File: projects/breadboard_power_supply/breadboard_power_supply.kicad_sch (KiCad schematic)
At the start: 17 parts, among them J1 Barrel_Jack_Switch, J2 Conn_01x03_Pin, J3 Conn_01x02_Pin, J4 Screw_Terminal_01x02, J5 Conn_01x03_Pin, J6 Conn_01x02_Pin, J7 Screw_Terminal_01x02, U1 LM7805_TO220, U2 LM317_TO-220

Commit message: Organize libraries, add footprints (WIP)
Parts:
- removed S1: OS102011MS2QN1, OS102011MS2QN1:SW_OS102011MS2QN1, symbol OS102011MS2QN1:OS102011MS2QN1
- added S1: OS102011MS2QN1, Slide_Switch:SW_OS102011MS2QN1, symbol MH_Slide_Switch_OS102011MS2QN1:OS102011MS2QN1
- C1, C2, C3: footprint (none) -> Capacitor_SMD:C_0603_1608Metric_Pad1.08x0.95mm_HandSolder
- J1: footprint (none) -> Connector_BarrelJack:BarrelJack_Kycon_KLDX-0202-xC_Horizontal
- R1, R2, R3: footprint (none) -> Resistor_SMD:R_0603_1608Metric_Pad0.98x0.95mm_HandSolder
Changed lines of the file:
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@@
-	)
-	(symbol
-		(lib_id "OS102011MS2QN1:OS102011MS2QN1")
-		(at 80.01 57.15 90)
-		(unit 1)
-		(exclude_from_sim no)
-		(in_bom yes)
-		(on_board yes)
-		(dnp no)
-		(fields_autoplaced yes)
-		(property "Reference" "S1"
-			(at 85.09 56.0069 90)
-			(effects
-				(font
-					(size 1.27 1.27)
-				)
-				(justify right)
-			)
-		)
-		(property "Value" "OS102011MS2QN1"
-			(at 85.09 58.5469 90)
-			(effects
-				(font
-					(size 1.27 1.27)
-				)
-				(justify right)
-			)
-		)
-		(property "Footprint" "OS102011MS2QN1:SW_OS102011MS2QN1"
-			(at 80.01 57.15 0)
-			(effects
-				(font
-					(size 1.27 1.27)
-				)
-				(justify bottom)
-				(hide yes)
-			)
-		)
-		(property "Datasheet" ""
-			(at 80.01 57.15 0)
-			(effects
-				(font
-					(size 1.27 1.27)
-				)
-				(hide yes)
-			)
-		)
-		(property "Description" ""
-			(at 80.01 57.15 0)
-			(effects
-				(font
-					(size 1.27 1.27)
-				)
-				(hide yes)
-			)
-		)
-		(property "STANDARD" "MANUFACTURER RECOMMENDATIONS"
-			(at 80.01 57.15 0)
-			(effects
-				(font
-					(size 1.27 1.27)
-				)
-				(justify bottom)
-				(hide yes)
-			)
-		)
-		(property "MANUFACTURER" "C&K"
-			(at 80.01 57.15 0)
-			(effects
-				(font
-					(size 1.27 1.27)
-				)
-				(justify bottom)
-				(hide yes)
-			)
-		)
-		(pin "3"
-		)
-		(pin "2"
-		)
-		(pin "1"
-		)
-		(instances
-			(project ""
-				(path "/7d501a1c-ecfc-4b89-8a82-881c56ebfdf1"
-					(reference "S1")
-					(unit 1)
-				)
-			)
-		)
 	)
 	(symbol
@@
 			)
 		)
-		(property "Footprint" ""
+		(property "Footprint" "Capacitor_SMD:C_0603_1608Metric_Pad1.08x0.95mm_HandSolder"
 			(at 111.76 75.2348 0)
 			(effects
@@
 			)
 		)
-		(property "Footprint" ""
+		(property "Footprint" "Connector_BarrelJack:BarrelJack_Kycon_KLDX-0202-xC_Horizontal"
 			(at 53.34 64.516 0)
 			(effects
@@
 			)
 		)
-		(property "Footprint" ""
+		(property "Footprint" "Resistor_SMD:R_0603_1608Metric_Pad0.98x0.95mm_HandSolder"
 			(at 107.188 133.35 90)
 			(effects
@@
 			)
 		)
-		(property "Footprint" ""
+		(property "Footprint" "Resistor_SMD:R_0603_1608Metric_Pad0.98x0.95mm_HandSolder"
 			(at 58.928 129.54 90)
 			(effects
@@
 			)
 		)
-		(property "Footprint" ""
+		(property "Footprint" "Capacitor_SMD:C_0603_1608Metric_Pad1.08x0.95mm_HandSolder"
 			(at 137.16 75.2348 0)
 			(effects
@@
 			)
 		)
-		(property "Footprint" ""
+		(property "Footprint" "Resistor_SMD:R_0603_1608Metric_Pad0.98x0.95mm_HandSolder"
 			(at 107.188 149.86 90)
 			(effects
@@
 			)
 		)
-		(property "Footprint" ""
+		(property "Footprint" "Capacitor_SMD:C_0603_1608Metric_Pad1.08x0.95mm_HandSolder"
 			(at 113.03 117.1448 0)
 			(effects
@@
 					(unit 1)
 				)
+			)
+		)
+	)
+	(symbol
+		(lib_id "MH_Slide_Switch_OS102011MS2QN1:OS102011MS2QN1")
+		(at 77.47 59.69 0)
+		(unit 1)
+		(exclude_from_sim no)
+		(in_bom yes)
+		(on_board yes)
+		(dnp no)
+		(fields_autoplaced yes)
+		(property "Reference" "S1"
+			(at 81.28 58.4199 0)
+			(effects
+				(font
+					(size 1.27 1.27)
+				)
+				(justify left)
+			)
+		)
+		(property "Value" "OS102011MS2QN1"
+			(at 81.28 60.9599 0)
+			(effects
+				(font
+					(size 1.27 1.27)
+				)
+				(justify left)
+			)
+		)
+		(property "Footprint" "Slide_Switch:SW_OS102011MS2QN1"
+			(at 77.47 59.69 0)
+			(effects
+				(font
+					(size 1.27 1.27)
+				)
+				(justify bottom)
+				(hide yes)
+			)
+		)
+		(property "Datasheet" ""
+			(at 77.47 59.69 0)
+			(effects
+				(font
+					(size 1.27 1.27)
+				)
+				(hide yes)
+			)
+		)
+		(property "Description" ""
+			(at 77.47 59.69 0)
+			(effects
+				(font
+					(size 1.27 1.27)
+				)
+				(hide yes)
+			)
+		)
+		(property "STANDARD" "MANUFACTURER RECOMMENDATIONS"
+			(at 77.47 59.69 0)
+			(effects
+				(font
+					(size 1.27 1.27)
+				)
+				(justify bottom)
+				(hide yes)
+			)
+		)
+		(property "MANUFACTURER" "C&K"
+			(at 77.47 59.69 0)
+			(effects
+				(font
+					(size 1.27 1.27)
+				)
+				(justify bottom)
+				(hide yes)
+			)
+		)
+		(pin "3"
+		)
+		(pin "1"
+		)
+		(pin "2"
+		)
+		(instances
+			(project ""
+				(path "/7d501a1c-ecfc-4b89-8a82-881c56ebfdf1"
+					(reference "S1")
+					(unit 1)
+				)

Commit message: Best practices for libraries in breadboard_power_supply project
- move libraries/ folder inside main project folder
- make paths references relative using ${KIPRJMOD} variable
- modify .gitignore to commit fp-lib-table and sym-lib-table
- update links to MH_Slider_Switch symbol and footprint in KiCAD files
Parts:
- S1: footprint Slide_Switch:SW_OS102011MS2QN1 -> MH_Slide_Switch:SW_OS102011MS2QN1; symbol MH_Slide_Switch_OS102011MS2QN1:OS102011MS2QN1 -> MH_Slide_Switch:OS102011MS2QN1
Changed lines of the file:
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@@
 	)
 	(symbol
-		(lib_id "MH_Slide_Switch_OS102011MS2QN1:OS102011MS2QN1")
+		(lib_id "MH_Slide_Switch:OS102011MS2QN1")
 		(at 77.47 59.69 0)
 		(unit 1)
@@
 			)
 		)
-		(property "Footprint" "Slide_Switch:SW_OS102011MS2QN1"
+		(property "Footprint" "MH_Slide_Switch:SW_OS102011MS2QN1"
 			(at 77.47 59.69 0)
 			(effects

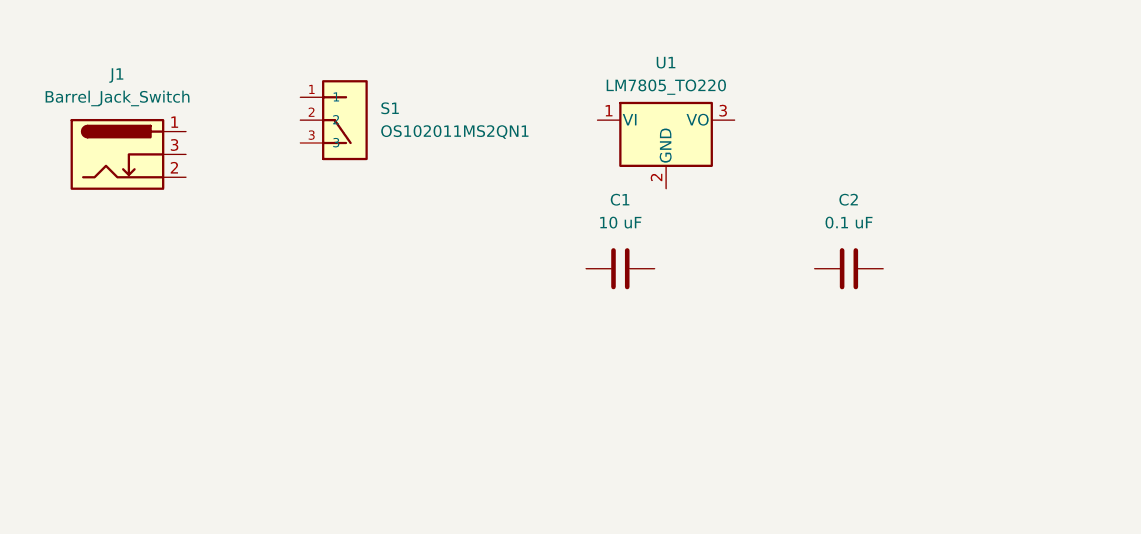
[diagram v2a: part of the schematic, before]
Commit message: Complete associations, start wiring
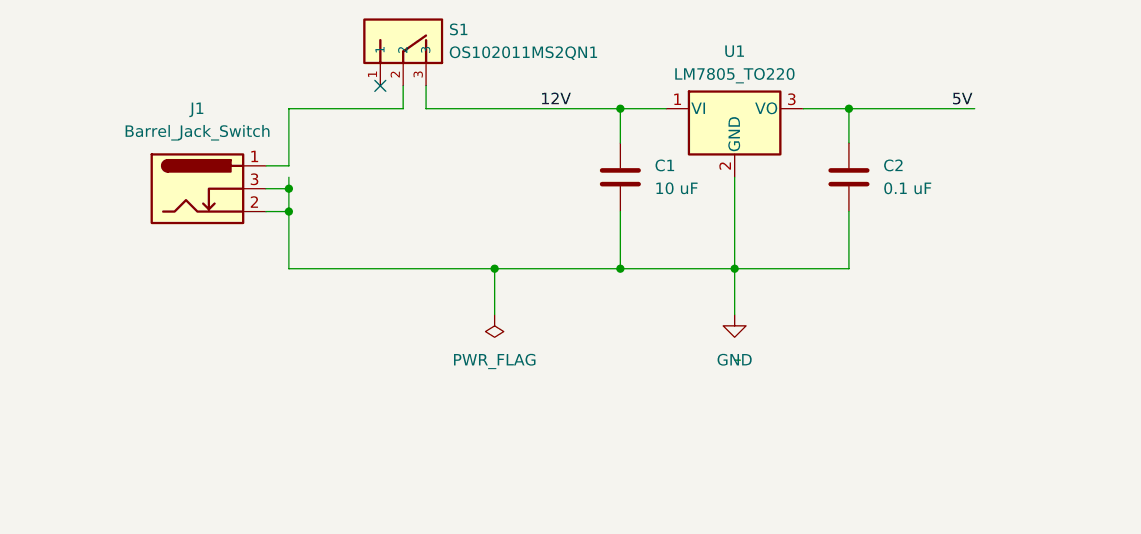
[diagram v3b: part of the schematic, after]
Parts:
- D1: footprint (none) -> LED_THT:LED_D5.0mm
- J2, J5: footprint (none) -> Connector_PinHeader_2.54mm:PinHeader_1x03_P2.54mm_Horizontal
- J3, J6: footprint (none) -> Connector_PinHeader_2.54mm:PinHeader_1x02_P2.54mm_Vertical
- J4, J7: footprint (none) -> TerminalBlock:TerminalBlock_bornier-2_P5.08mm
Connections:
- net GND: now reaches C1.1
- net GND: now also C2.1, J1.2, J1.3, U1.2 (GND)
- net 12V: now reaches C1.2
- net 12V: now also S1.3, U1.1 (VI)
- net at J1.1: now also S1.2
- net 5V: now reaches U1.3 (VO)
- net 5V: now also C2.2
- no-connect marks 0 -> 1
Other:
- moved on the sheet: C1, C2, J1, S1, U1

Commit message: Complete wiring
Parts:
- renumbered J7 to J6, J6 to J7, U2 to U1, U1 to U2
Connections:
- net 12V: now also R1.1, S1.1, U1.3 (VI); no longer S1.3
- net 5V: now also J2.3 (Pin_3), J5.3 (Pin_3)
- net GND: now also C3.1, D1.1 (K), J3.1 (Pin_1), J4.1 (Pin_1), J6.1 (Pin_1), J7.1 (Pin_1), R3.1
- net at J7.2 (Pin_2): now also J5.2 (Pin_2), J6.2 (Pin_2)
- net 3.3V: now reaches J5.1 (Pin_1)
- net 3.3V: now also C3.2, J2.1 (Pin_1), R2.2, U1.2 (VO)
- net at J2.2 (Pin_2): now also J3.2 (Pin_2), J4.2 (Pin_2)
- net at R2.1: now also R3.2, U1.1 (ADJ)
- net at R1.2: now also D1.2 (A)
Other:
- moved on the sheet: C1, C2, C3, D1, J1, J2, J3, J4, J5, J6, J7, R1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

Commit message: Name Nets
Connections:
- net PWR_output: now reaches J5.2 (Pin_2), J6.2 (Pin_2), J7.2 (Pin_2)
- net PWR_output: now also J2.2 (Pin_2), J3.2 (Pin_2), J4.2 (Pin_2)
- net PWR_input: now reaches J1.1, S1.2
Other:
- moved on the sheet: D1
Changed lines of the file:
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@@
 	)
 	(junction
-		(at 179.07 71.12)
+		(at 180.34 71.12)
 		(diameter 0)
 		(color 0 0 0 0)
@@
 	)
 	(junction
-		(at 184.15 59.69)
+		(at 185.42 59.69)
 		(diameter 0)
 		(color 0 0 0 0)
@@
 	(wire
 		(pts
-			(xy 179.07 62.23) (xy 190.5 62.23)
+			(xy 180.34 62.23) (xy 190.5 62.23)
 		)
 		(stroke
@@
 	(wire
 		(pts
-			(xy 179.07 71.12) (xy 190.5 71.12)
+			(xy 180.34 71.12) (xy 190.5 71.12)
 		)
 		(stroke
@@
 	(wire
 		(pts
-			(xy 184.15 46.99) (xy 184.15 59.69)
-		)
-		(stroke
-			(width 0)
-			(type default)
-		)
-	)
-	(wire
-		(pts
-			(xy 190.5 46.99) (xy 184.15 46.99)
+			(xy 185.42 46.99) (xy 185.42 59.69)
+		)
+		(stroke
+			(width 0)
+			(type default)
+		)
+	)
+	(wire
+		(pts
+			(xy 190.5 46.99) (xy 185.42 46.99)
 		)
 		(stroke
@@
 	(wire
 		(pts
-			(xy 179.07 62.23) (xy 179.07 71.12)
-		)
-		(stroke
-			(width 0)
-			(type default)
-		)
-	)
-	(wire
-		(pts
-			(xy 184.15 68.58) (xy 190.5 68.58)
+			(xy 180.34 62.23) (xy 180.34 71.12)
+		)
+		(stroke
+			(width 0)
+			(type default)
+		)
+	)
+	(wire
+		(pts
+			(xy 185.42 68.58) (xy 190.5 68.58)
 		)
 		(stroke
@@
 	(wire
 		(pts
-			(xy 179.07 71.12) (xy 179.07 77.47)
+			(xy 180.34 71.12) (xy 180.34 77.47)
 		)
 		(stroke
@@
 	(wire
 		(pts
-			(xy 184.15 59.69) (xy 190.5 59.69)
+			(xy 185.42 59.69) (xy 190.5 59.69)
 		)
 		(stroke
@@
 	(wire
 		(pts
-			(xy 184.15 59.69) (xy 184.15 68.58)
-		)
-		(stroke
-			(width 0)
-			(type default)
+			(xy 185.42 59.69) (xy 185.42 68.58)
+		)
+		(stroke
+			(width 0)
+			(type default)
+		)
+	)
+	(label "PWR_input"
+		(at 48.26 41.91 180)
+		(effects
+			(font
+				(size 1.27 1.27)
+			)
+			(justify right bottom)
 		)
 	)
@@
 		)
 	)
+	(label "PWR_output"
+		(at 185.42 110.49 180)
+		(effects
+			(font
+				(size 1.27 1.27)
+			)
+			(justify right bottom)
+		)
+	)
 	(label "3.3V"
 		(at 191.77 100.33 180)
@@
 		)
 	)
+	(label "PWR_output"
+		(at 185.42 59.69 180)
+		(effects
+			(font
+				(size 1.27 1.27)
+			)
+			(justify right bottom)
+		)
+	)
 	(label "12V"
 		(at 54.61 102.87 0)
@@
 	(symbol
 		(lib_id "power:GND")
-		(at 179.07 77.47 0)
+		(at 180.34 77.47 0)
 		(unit 1)
 		(exclude_from_sim no)
@@
 		(fields_autoplaced yes)
 		(property "Reference" "#PWR03"
-			(at 179.07 83.82 0)
+			(at 180.34 83.82 0)
 			(effects
 				(font
@@
 		)
 		(property "Value" "GND"
-			(at 179.07 82.55 0)
+			(at 180.34 82.55 0)
 			(effects
 				(font
@@
 		)
 		(property "Footprint" ""
-			(at 179.07 77.47 0)
+			(at 180.34 77.47 0)
 			(effects
 				(font
@@
 		)
 		(property "Datasheet" ""
-			(at 179.07 77.47 0)
+			(at 180.34 77.47 0)
 			(effects
 				(font
@@
 		)
 		(property "Description" "Power symbol creates a global label with name \"GND\" , ground"
-			(at 179.07 77.47 0)
+			(at 180.34 77.47 0)
 			(effects
 				(font
@@
 	(symbol
 		(lib_id "Device:LED")
-		(at 80.01 129.54 0)
-		(mirror y)
+		(at 80.01 129.54 180)
 		(unit 1)
 		(exclude_from_sim no)
@@
 		(dnp no)
 		(property "Reference" "D1"
-			(at 81.5975 137.16 0)
+			(at 81.5975 121.92 0)
 			(effects
 				(font
@@
 		)
 		(property "Value" "LED"
-			(at 81.5975 134.62 0)
-			(effects
-				(font
+			(at 81.5975 124.46 0)
+			(effects
+				(font

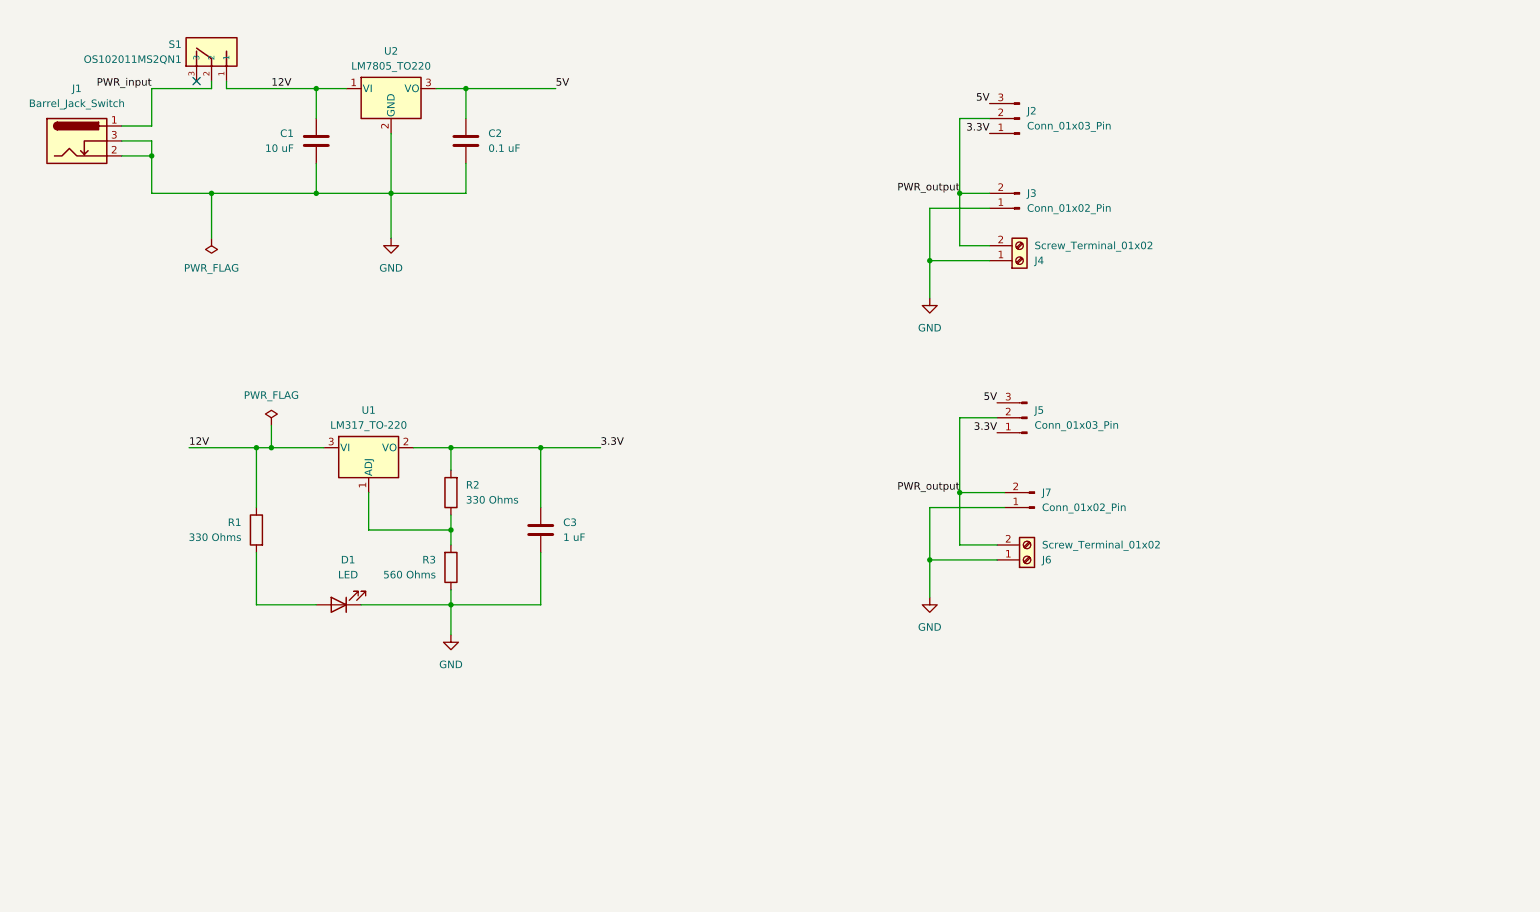
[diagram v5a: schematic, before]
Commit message: Define net classes, add text and boxes, improve logo
- Add net classes
- Add boxes, text, and graphics to the drawing sheet
- improve color version of logo: blacker lines, round
  junction on the left, clean background
- make b/w version of logo in BMP and then .kicad_mod
  using Image Converter to use as silkscreen logo
- make b/w version in SVG to add as graphic to the
  drawing sheet
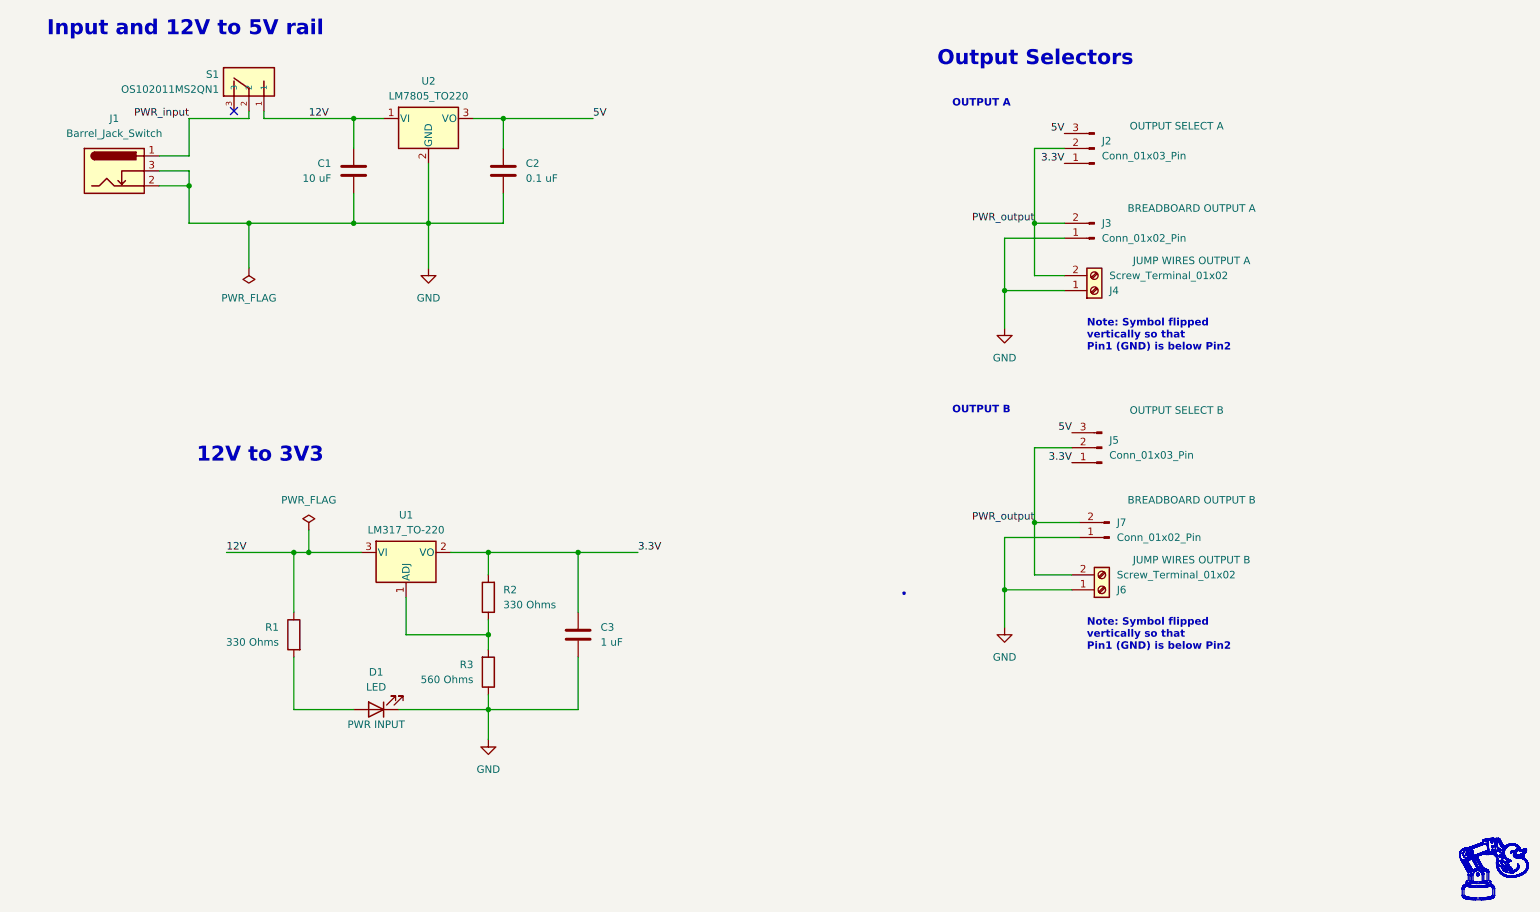
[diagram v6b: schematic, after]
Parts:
- D1: My_Label (none) -> PWR INPUT
- J2: My_Label (none) -> OUTPUT SELECT A
- J3: My_Label (none) -> BREADBOARD OUTPUT A
- J4: My_Label (none) -> JUMP WIRES OUTPUT A
- J5: My_Label (none) -> OUTPUT SELECT B
- J6: My_Label (none) -> JUMP WIRES OUTPUT B
- J7: My_Label (none) -> BREADBOARD OUTPUT B
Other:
- note added: "12V to 3V3"
- note added: "Input and 12V to 5V rail"
- note added: "Note: Symbol flipped vertically so that Pin1 (GND) is below Pin2"
- note added: "OUTPUT A"
- note added: "OUTPUT B"
- note added: "Output Selectors"
- moved on the sheet: C1, C2, C3, D1, J1, J2, J3, J4, J5, J6, J7, R1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
